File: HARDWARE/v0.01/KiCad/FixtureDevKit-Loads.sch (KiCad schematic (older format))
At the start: 24 parts, among them J30 LOAD_0, J31 LOAD_1, J32 LOAD_2, J33 LOAD_3, Q1 NTF2955T1G, Q2 NTF2955T1G, Q3 NTF2955T1G, Q4 NTF2955T1G

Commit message: beginning pcb layout
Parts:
- R45: footprint Resistors_SMD:R_0805_HandSoldering -> Resistors_THT:R_Axial_Power_L25.0mm_W9.0mm_P30.48mm
- R46, R47, R48: footprint (none) -> Resistors_THT:R_Axial_Power_L25.0mm_W9.0mm_P30.48mm
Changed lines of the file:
@@
 F 0 "R45" V 2580 3800 50  0000 C CNN
 F 1 "10R, 5W" V 2500 3800 50  0000 C CNN
-F 2 "Resistors_SMD:R_0805_HandSoldering" V 2430 3800 50  0001 C CNN
+F 2 "Resistors_THT:R_Axial_Power_L25.0mm_W9.0mm_P30.48mm" V 2430 3800 50  0001 C CNN
 F 3 "" H 2500 3800 50  0001 C CNN
 	1    2500 3800
@@
 F 0 "R46" V 4480 3800 50  0000 C CNN
 F 1 "10R, 5W" V 4400 3800 50  0000 C CNN
-F 2 "" V 4330 3800 50  0001 C CNN
+F 2 "Resistors_THT:R_Axial_Power_L25.0mm_W9.0mm_P30.48mm" V 4330 3800 50  0001 C CNN
 F 3 "" H 4400 3800 50  0001 C CNN
 	1    4400 3800
@@
 F 0 "R47" V 6380 3800 50  0000 C CNN
 F 1 "10R, 5W" V 6300 3800 50  0000 C CNN
-F 2 "" V 6230 3800 50  0001 C CNN
+F 2 "Resistors_THT:R_Axial_Power_L25.0mm_W9.0mm_P30.48mm" V 6230 3800 50  0001 C CNN
 F 3 "" H 6300 3800 50  0001 C CNN
 	1    6300 3800
@@
 F 0 "R48" V 8280 3800 50  0000 C CNN
 F 1 "10R, 5W" V 8200 3800 50  0000 C CNN
-F 2 "" V 8130 3800 50  0001 C CNN
+F 2 "Resistors_THT:R_Axial_Power_L25.0mm_W9.0mm_P30.48mm" V 8130 3800 50  0001 C CNN
 F 3 "" H 8200 3800 50  0001 C CNN
 	1    8200 3800

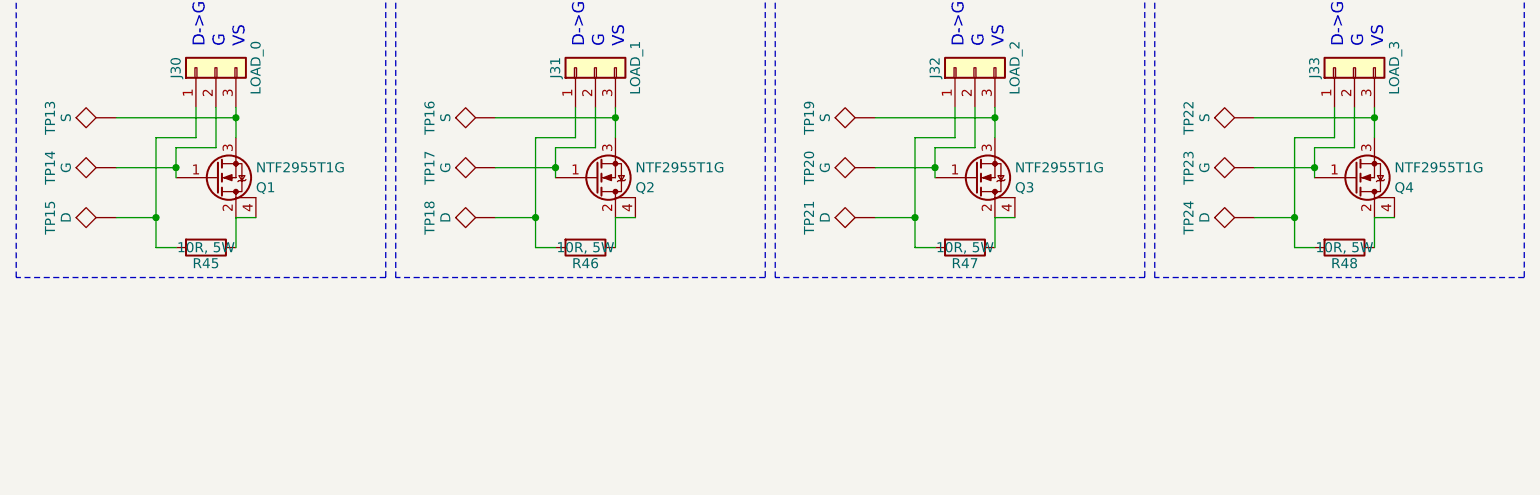
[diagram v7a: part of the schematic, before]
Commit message: adding datasheets and laying out PCB
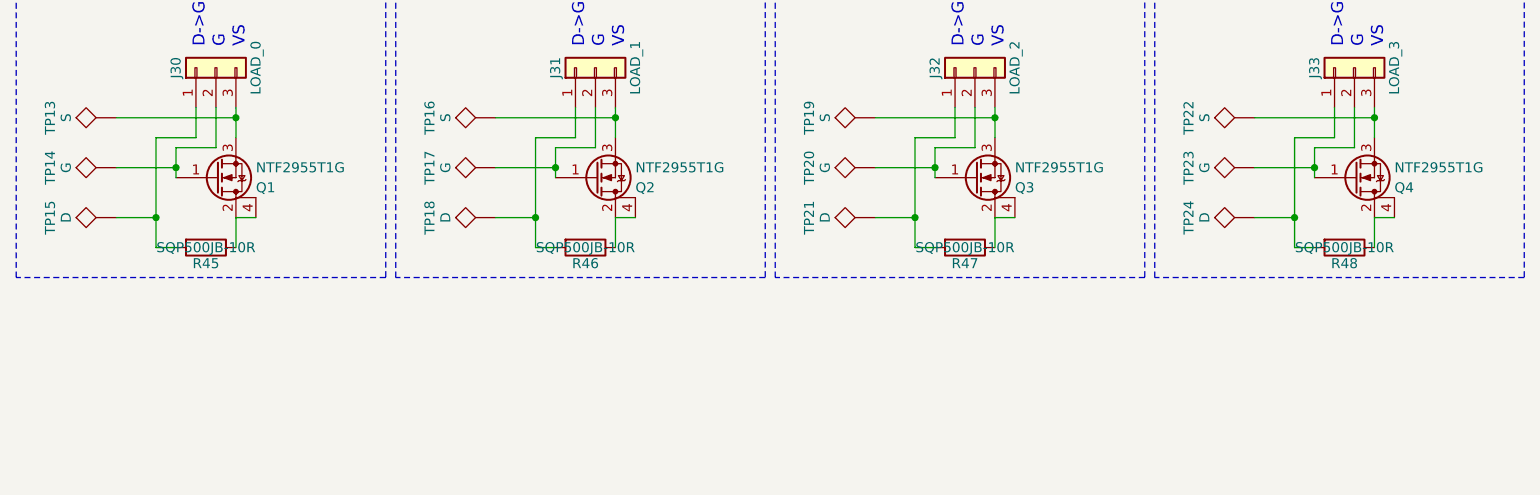
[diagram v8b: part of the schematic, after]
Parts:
- R45, R46, R47, R48: value 10R, 5W -> SQP500JB-10R; footprint Resistors_THT:R_Axial_Power_L25.0mm_W9.0mm_P30.48mm -> RES_TWM3J560E:RES_TWM3J560E
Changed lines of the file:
@@
 LIBS:valves
 LIBS:TCA6424ARGJR
+LIBS:USB-A1HSW6
 LIBS:Fixture-Dev-Kit-cache
 EELAYER 25 0
@@
 P 2500 3800
 F 0 "R45" V 2580 3800 50  0000 C CNN
-F 1 "10R, 5W" V 2500 3800 50  0000 C CNN
-F 2 "Resistors_THT:R_Axial_Power_L25.0mm_W9.0mm_P30.48mm" V 2430 3800 50  0001 C CNN
+F 1 "SQP500JB-10R" V 2500 3800 50  0000 C CNN
+F 2 "RES_TWM3J560E:RES_TWM3J560E" V 2430 3800 50  0001 C CNN
 F 3 "" H 2500 3800 50  0001 C CNN
 	1    2500 3800
@@
 P 4400 3800
 F 0 "R46" V 4480 3800 50  0000 C CNN
-F 1 "10R, 5W" V 4400 3800 50  0000 C CNN
-F 2 "Resistors_THT:R_Axial_Power_L25.0mm_W9.0mm_P30.48mm" V 4330 3800 50  0001 C CNN
+F 1 "SQP500JB-10R" V 4400 3800 50  0000 C CNN
+F 2 "RES_TWM3J560E:RES_TWM3J560E" V 4330 3800 50  0001 C CNN
 F 3 "" H 4400 3800 50  0001 C CNN
 	1    4400 3800
@@
 P 6300 3800
 F 0 "R47" V 6380 3800 50  0000 C CNN
-F 1 "10R, 5W" V 6300 3800 50  0000 C CNN
-F 2 "Resistors_THT:R_Axial_Power_L25.0mm_W9.0mm_P30.48mm" V 6230 3800 50  0001 C CNN
+F 1 "SQP500JB-10R" V 6300 3800 50  0000 C CNN
+F 2 "RES_TWM3J560E:RES_TWM3J560E" V 6230 3800 50  0001 C CNN
 F 3 "" H 6300 3800 50  0001 C CNN
 	1    6300 3800
@@
 P 8200 3800
 F 0 "R48" V 8280 3800 50  0000 C CNN
-F 1 "10R, 5W" V 8200 3800 50  0000 C CNN
-F 2 "Resistors_THT:R_Axial_Power_L25.0mm_W9.0mm_P30.48mm" V 8130 3800 50  0001 C CNN
+F 1 "SQP500JB-10R" V 8200 3800 50  0000 C CNN
+F 2 "RES_TWM3J560E:RES_TWM3J560E" V 8130 3800 50  0001 C CNN
 F 3 "" H 8200 3800 50  0001 C CNN
 	1    8200 3800
